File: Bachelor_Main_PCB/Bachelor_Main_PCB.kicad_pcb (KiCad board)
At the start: 2 copper layers, 3 parts, among them J1 F32Q-1A7H1-11022, U1 SC0683

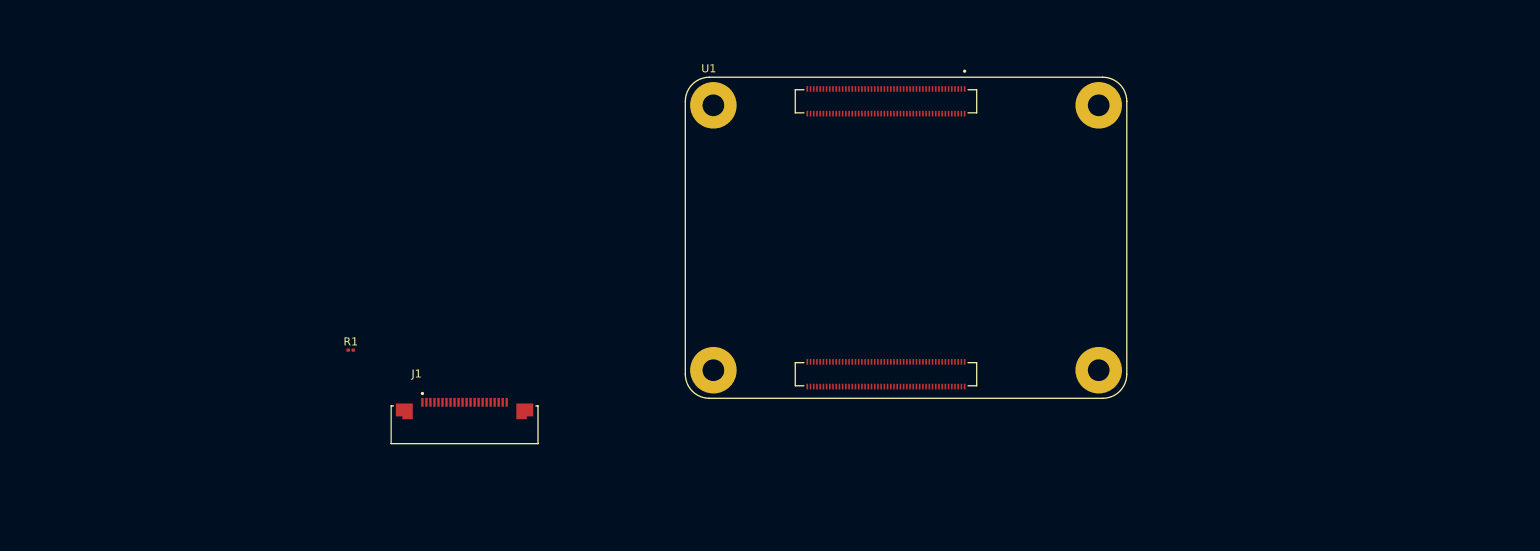
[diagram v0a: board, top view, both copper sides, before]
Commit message: Add Spacers for RPI CM and created separate hierarchical sheets
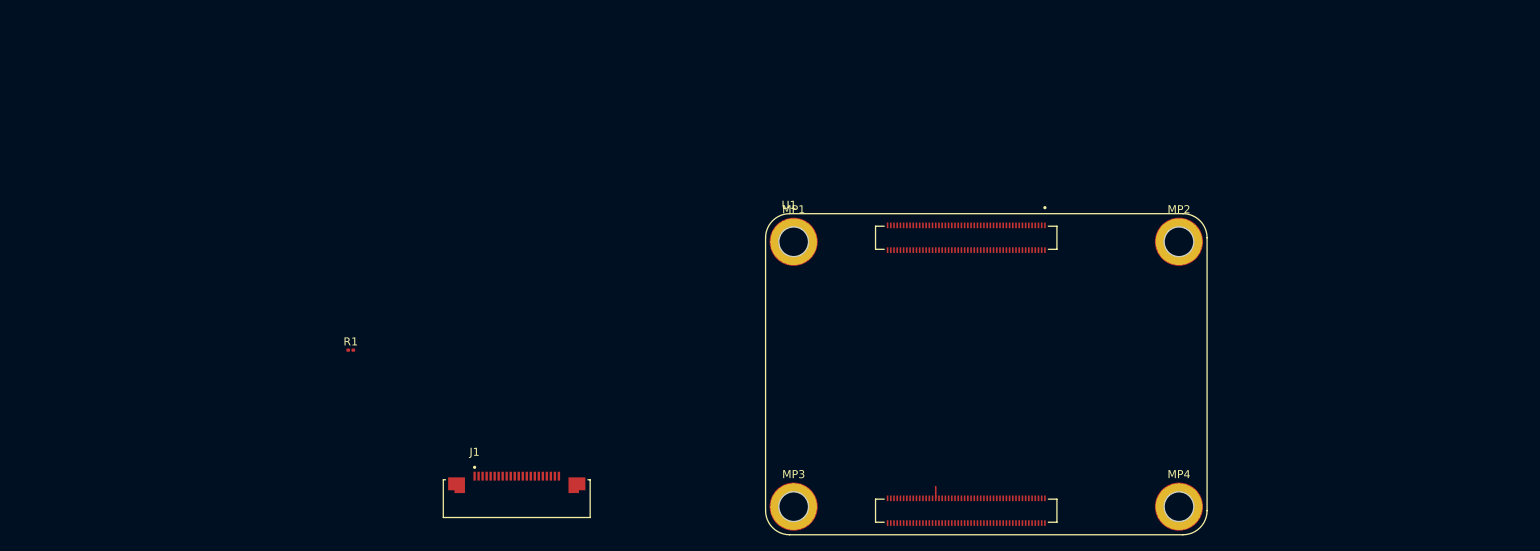
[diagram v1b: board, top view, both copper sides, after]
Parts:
- added MP1: WA-SMSI_9774XXX151, WA-SMSI_9774XXX151:WA-SMSI_9774030151, F.Cu at (159.0, 67.5)
- added MP2: WA-SMSI_9774XXX151, WA-SMSI_9774XXX151:WA-SMSI_9774030151, F.Cu at (207.0, 67.5)
- added MP3: WA-SMSI_9774XXX151, WA-SMSI_9774XXX151:WA-SMSI_9774030151, F.Cu at (159.0, 100.5)
- added MP4: WA-SMSI_9774XXX151, WA-SMSI_9774XXX151:WA-SMSI_9774030151, F.Cu at (207.0, 100.5)
- moved U1 19.7 mm to (183.0, 84.0)
- moved J1 11.3 mm to (124.5, 99.5)
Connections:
- J1 pad 1: unconnected-(J1-Pad1) -> SD-pin6
- J1 pad 10: unconnected-(J1-Pad10) -> SD-pin5
- J1 pad 11: unconnected-(J1-Pad11) -> SD-pin6
- J1 pad 12: unconnected-(J1-Pad12) -> SD-pin4
- J1 pad 13: unconnected-(J1-Pad13) -> SD-pin4
- J1 pad 14: unconnected-(J1-Pad14) -> SD-pin6
- J1 pad 15: unconnected-(J1-Pad15) -> SD-pin3
- J1 pad 16: unconnected-(J1-Pad16) -> SD-pin3
- J1 pad 17: unconnected-(J1-Pad17) -> SD-pin6
- J1 pad 18: unconnected-(J1-Pad18) -> SD-pin2
- J1 pad 19: unconnected-(J1-Pad19) -> SD-pin2
- J1 pad 2: unconnected-(J1-Pad2) -> SD-pin6
- J1 pad 20: unconnected-(J1-Pad20) -> SD-pin6
- J1 pad 21: unconnected-(J1-Pad21) -> SD-pin1
- J1 pad 22: unconnected-(J1-Pad22) -> SD-pin1
- J1 pad 3: unconnected-(J1-Pad3) -> SD-pin8
- J1 pad 4: unconnected-(J1-Pad4) -> SD-pin8
- J1 pad 5: unconnected-(J1-Pad5) -> SD-pin6
- J1 pad 6: unconnected-(J1-Pad6) -> SD-pin7
- J1 pad 7: unconnected-(J1-Pad7) -> SD-pin7
- J1 pad 8: unconnected-(J1-Pad8) -> SD-pin6
- J1 pad 9: unconnected-(J1-Pad9) -> SD-pin5
- R1 pad 2: GND -> SD-pin6
- U1 pad 1: Net-(U1A-GND-Pad1) -> SD-pin6
- U1 pad 107: Net-(U1A-GND-Pad1) -> SD-pin6
- U1 pad 108: Net-(U1A-GND-Pad1) -> SD-pin6
- U1 pad 113: Net-(U1A-GND-Pad1) -> SD-pin6
- U1 pad 114: Net-(U1A-GND-Pad1) -> SD-pin6
- U1 pad 119: Net-(U1A-GND-Pad1) -> SD-pin6
- U1 pad 120: Net-(U1A-GND-Pad1) -> SD-pin6
- U1 pad 125: Net-(U1A-GND-Pad1) -> SD-pin6
- U1 pad 126: Net-(U1A-GND-Pad1) -> SD-pin6
- U1 pad 13: Net-(U1A-GND-Pad1) -> SD-pin6
- U1 pad 131: Net-(U1A-GND-Pad1) -> SD-pin6
- U1 pad 132: Net-(U1A-GND-Pad1) -> SD-pin6
- U1 pad 137: Net-(U1A-GND-Pad1) -> SD-pin6
- U1 pad 138: Net-(U1A-GND-Pad1) -> SD-pin6
- U1 pad 14: Net-(U1A-GND-Pad1) -> SD-pin6
- U1 pad 144: Net-(U1A-GND-Pad1) -> SD-pin6
- U1 pad 150: Net-(U1A-GND-Pad1) -> SD-pin6
- U1 pad 155: Net-(U1A-GND-Pad1) -> SD-pin6
- U1 pad 156: Net-(U1A-GND-Pad1) -> SD-pin6
- U1 pad 161: Net-(U1A-GND-Pad1) -> SD-pin6
- U1 pad 162: Net-(U1A-GND-Pad1) -> SD-pin6
- U1 pad 167: Net-(U1A-GND-Pad1) -> SD-pin6
- U1 pad 168: Net-(U1A-GND-Pad1) -> SD-pin6
- U1 pad 173: Net-(U1A-GND-Pad1) -> SD-pin6
- U1 pad 174: Net-(U1A-GND-Pad1) -> SD-pin6
- U1 pad 179: Net-(U1A-GND-Pad1) -> SD-pin6
- U1 pad 180: Net-(U1A-GND-Pad1) -> SD-pin6
- U1 pad 185: Net-(U1A-GND-Pad1) -> SD-pin6
- U1 pad 186: Net-(U1A-GND-Pad1) -> SD-pin6
- U1 pad 191: Net-(U1A-GND-Pad1) -> SD-pin6
- U1 pad 192: Net-(U1A-GND-Pad1) -> SD-pin6
- U1 pad 197: Net-(U1A-GND-Pad1) -> SD-pin6
- U1 pad 198: Net-(U1A-GND-Pad1) -> SD-pin6
- U1 pad 2: Net-(U1A-GND-Pad1) -> SD-pin6
- U1 pad 22: Net-(U1A-GND-Pad1) -> SD-pin6
- U1 pad 23: Net-(U1A-GND-Pad1) -> SD-pin6
- U1 pad 32: Net-(U1A-GND-Pad1) -> SD-pin6
- U1 pad 33: Net-(U1A-GND-Pad1) -> SD-pin6
- U1 pad 42: Net-(U1A-GND-Pad1) -> SD-pin6
- U1 pad 43: Net-(U1A-GND-Pad1) -> SD-pin6
- U1 pad 52: Net-(U1A-GND-Pad1) -> SD-pin6
- U1 pad 53: Net-(U1A-GND-Pad1) -> SD-pin6
- U1 pad 59: Net-(U1A-GND-Pad1) -> SD-pin6
- U1 pad 60: Net-(U1A-GND-Pad1) -> SD-pin6
- U1 pad 65: Net-(U1A-GND-Pad1) -> SD-pin6
- U1 pad 66: Net-(U1A-GND-Pad1) -> SD-pin6
- U1 pad 7: Net-(U1A-GND-Pad1) -> SD-pin6
- U1 pad 71: Net-(U1A-GND-Pad1) -> SD-pin6
- U1 pad 74: Net-(U1A-GND-Pad1) -> SD-pin6
- U1 pad 8: Net-(U1A-GND-Pad1) -> SD-pin6
- U1 pad 98: Net-(U1A-GND-Pad1) -> SD-pin6
- U1 pad SH1: Net-(U1A-MOUNTING_PADS-PadSH1) -> SD-pin6
- U1 pad SH2: Net-(U1A-MOUNTING_PADS-PadSH1) -> SD-pin6
- U1 pad SH3: Net-(U1A-MOUNTING_PADS-PadSH1) -> SD-pin6
- U1 pad SH4: Net-(U1A-MOUNTING_PADS-PadSH1) -> SD-pin6
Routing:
- net unconnected-(U1B-DSI0_C_N-Pad169): track 0.00 -> 1.46 mm

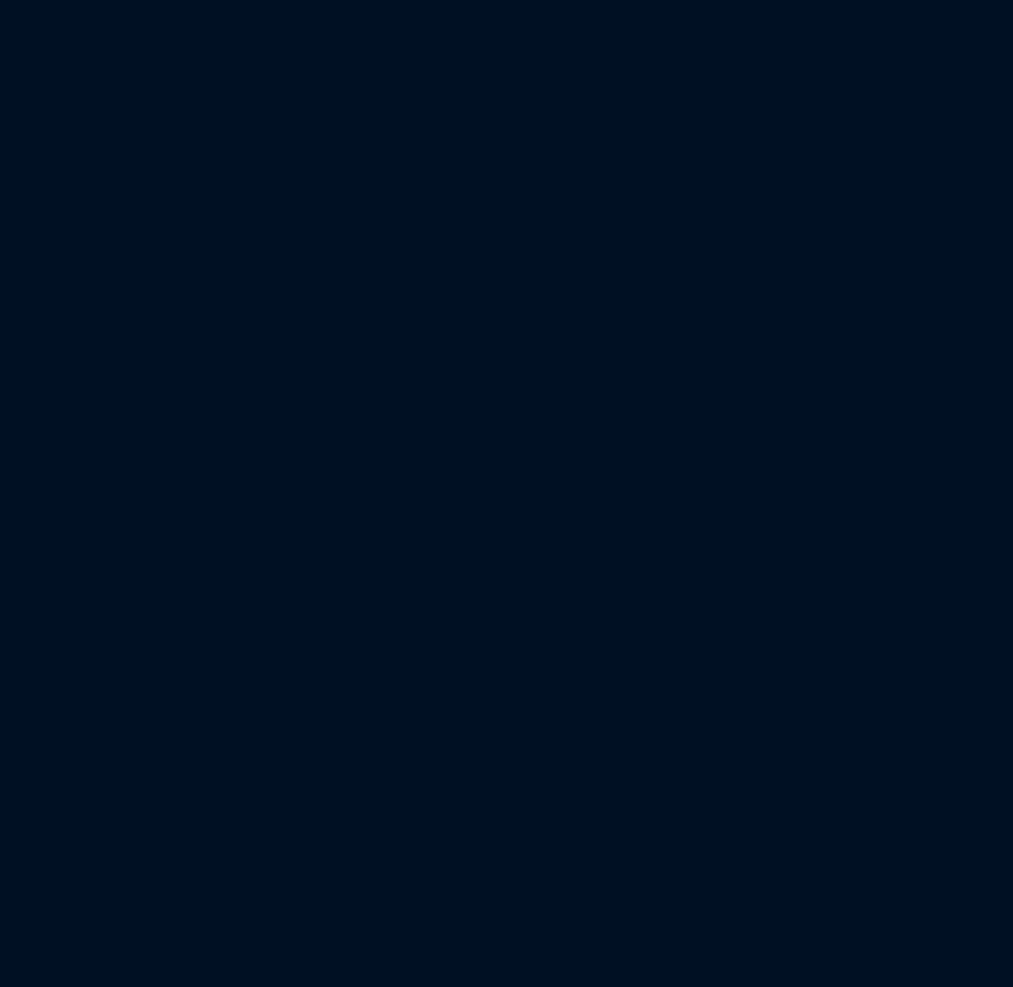
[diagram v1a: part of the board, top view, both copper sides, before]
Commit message: Add Sierra Wireless modem and 100pin RPI CM connectors
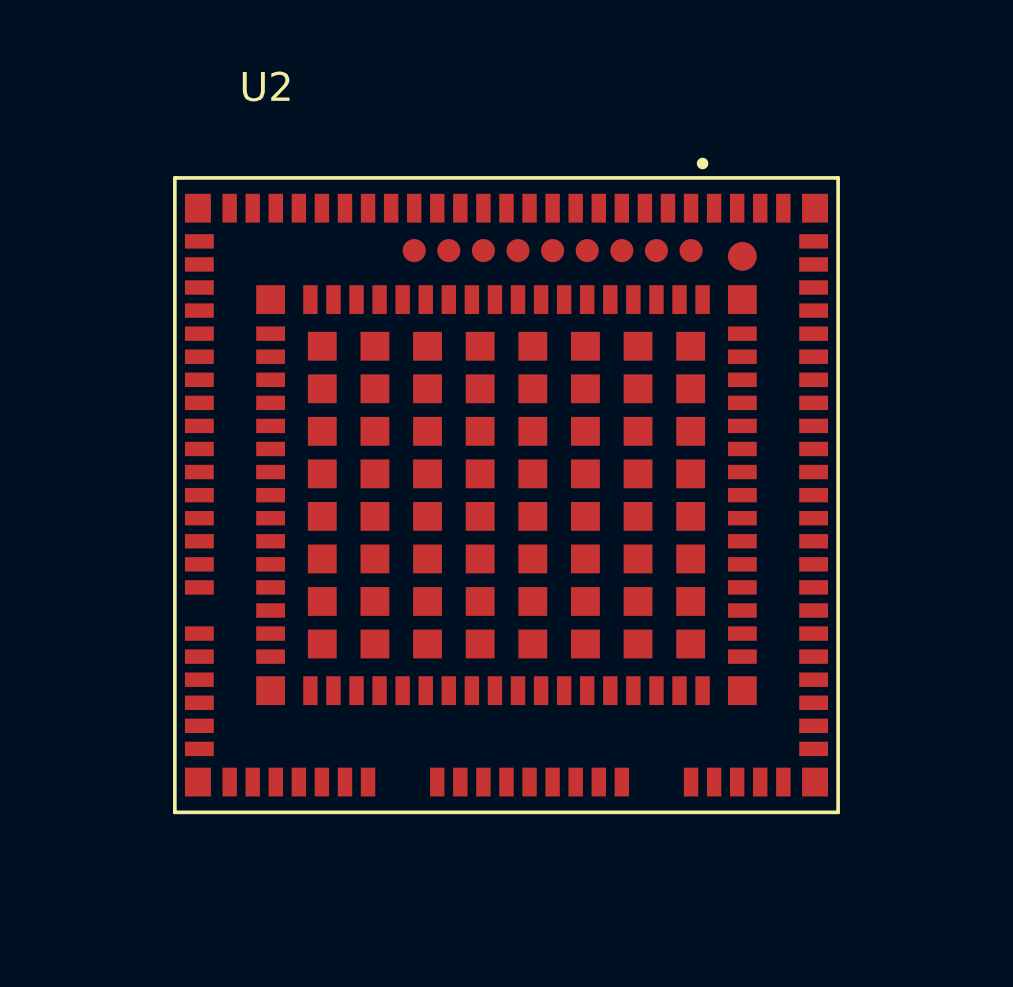
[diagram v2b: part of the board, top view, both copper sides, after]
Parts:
- added U2: RC7620_1104625, RC7620_1104625:XCVR_RC7620_1104625, F.Cu at (124.3, 54.5)

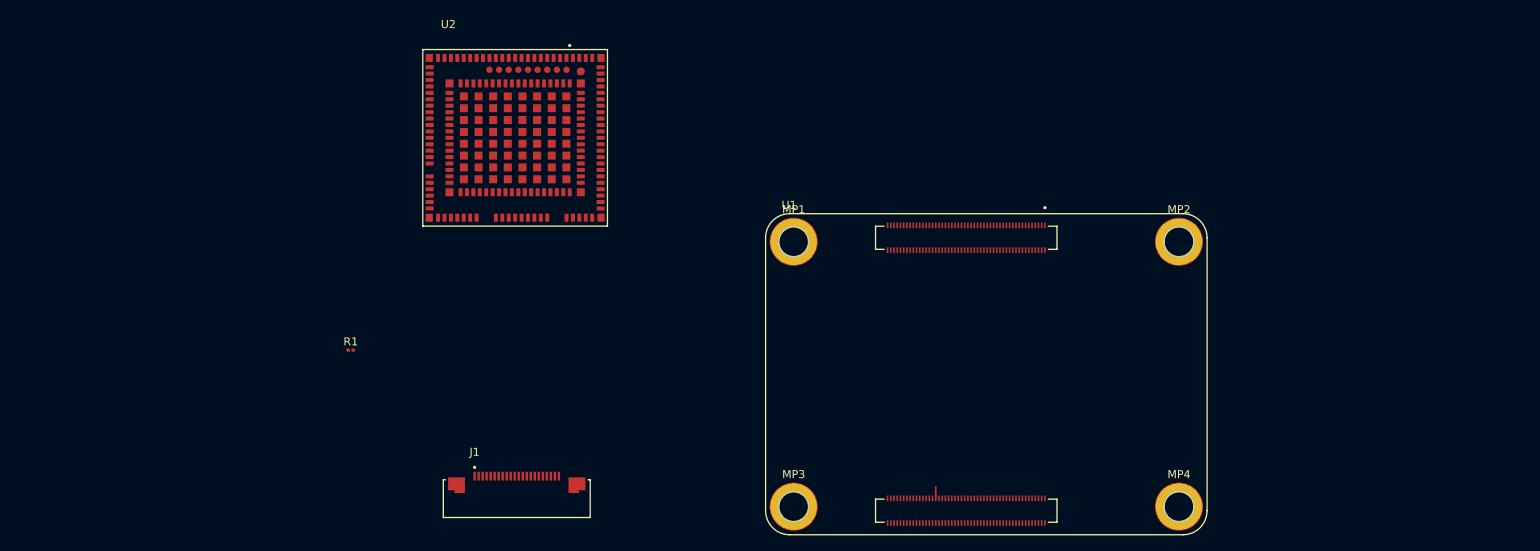
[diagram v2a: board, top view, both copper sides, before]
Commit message: Add STM32 and 3d model. Made power suply sheet
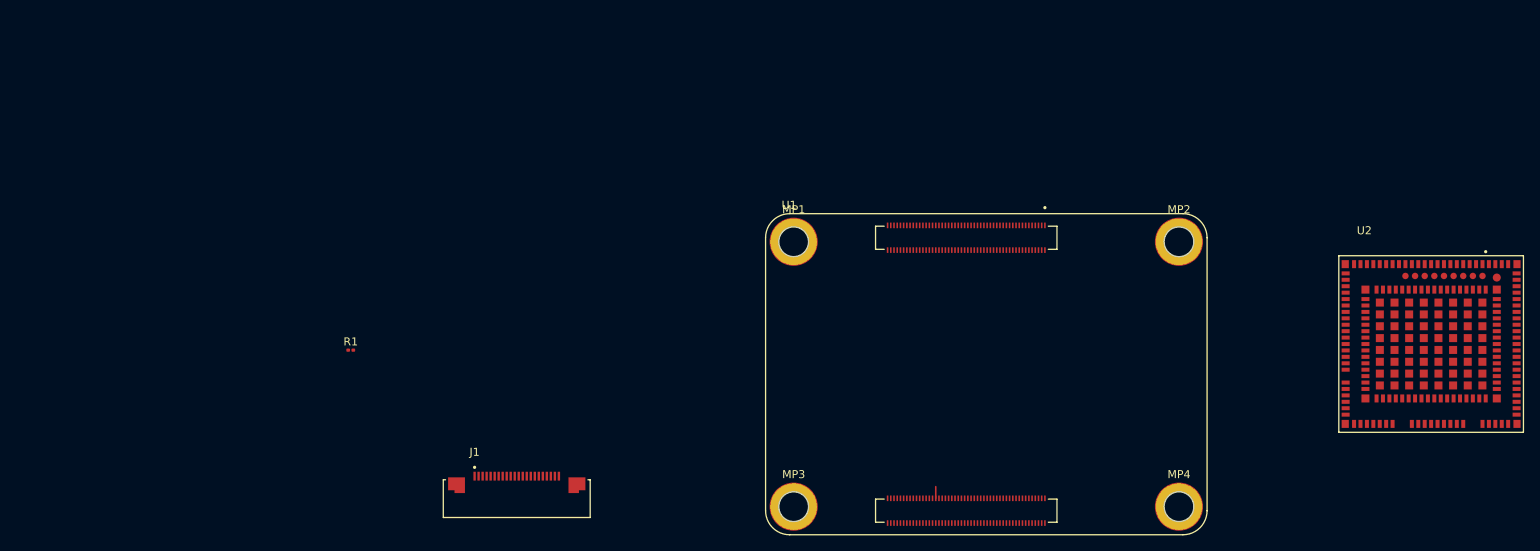
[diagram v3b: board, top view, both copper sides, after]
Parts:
- moved U2 117.0 mm to (238.4, 80.2)
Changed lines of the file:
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@@
+			)
+		)
+		(model "${KICAD9_3DMODEL_DIR}/DF40HC_3.0_-100DS-0.4V_58/DF40HC_3.0_-100DS-0.4V_58.step"
+			(offset
+				(xyz -2.5 -17 0)
+			)
+			(scale
+				(xyz 1 1 1)
+			)
+			(rotate
+				(xyz -90 -0 -0)
+			)
+		)
+		(model "${KICAD9_3DMODEL_DIR}/DF40HC_3.0_-100DS-0.4V_58/DF40HC_3.0_-100DS-0.4V_58.step"
+			(offset
+				(xyz -2.5 17 0)
+			)
+			(scale
+				(xyz 1 1 1)
+			)
+			(rotate
+				(xyz -90 -0 -0)
 			)
 		)
@@
 	(footprint "RC7620_1104625:XCVR_RC7620_1104625"
 		(layer "F.Cu")
-		(at 124.3 54.55)
+		(at 238.4125 80.2375)
 		(property "Reference" "U2"
 			(at -8.325 -14.135 0)

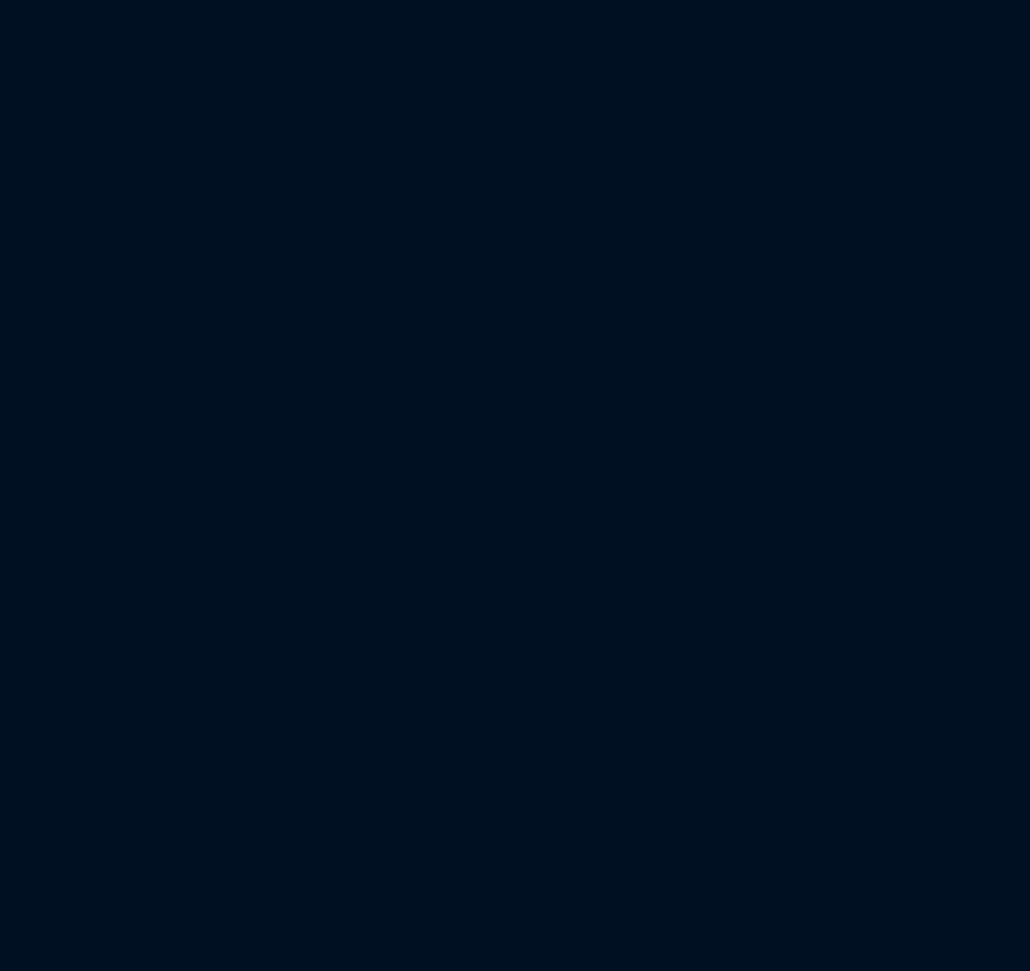
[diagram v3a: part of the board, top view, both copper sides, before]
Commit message: Add STM32 3D modell
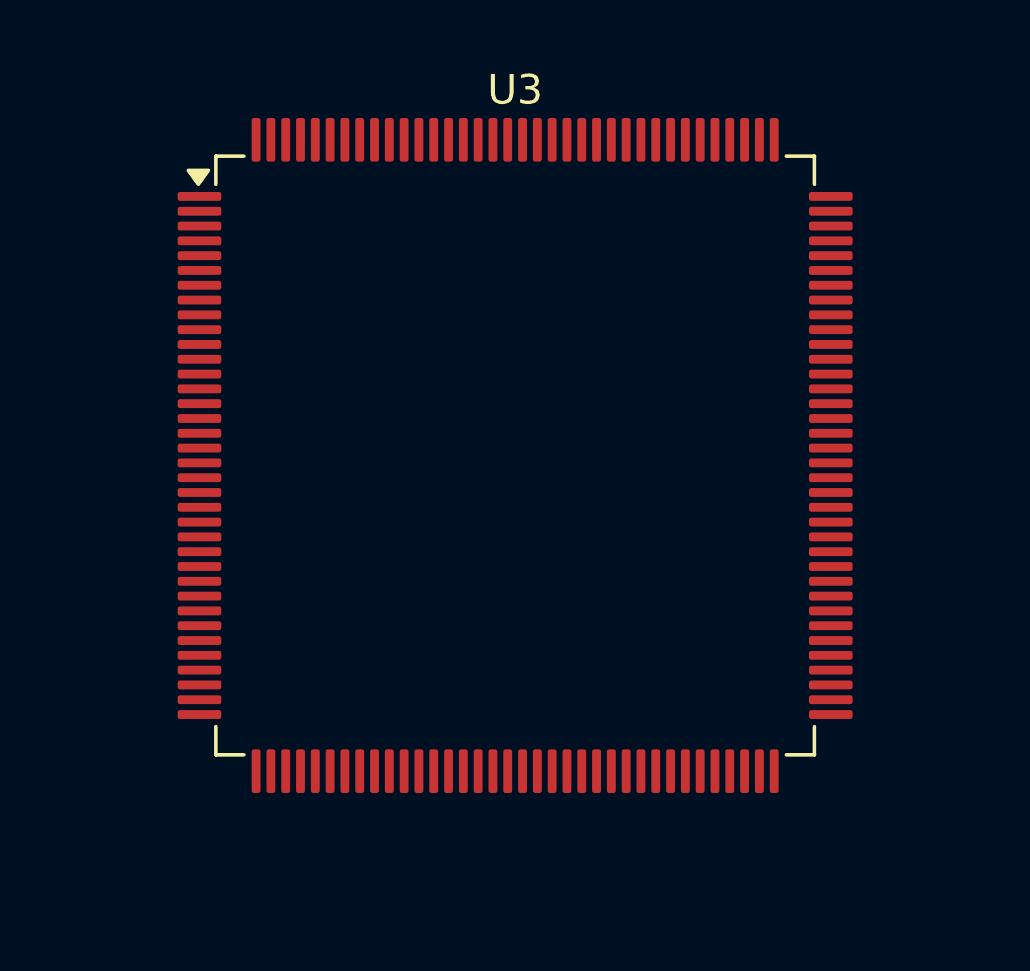
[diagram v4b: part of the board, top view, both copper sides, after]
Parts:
- added U3: STM32H7A3ZITxQ, Package_QFP:LQFP-144_20x20mm_P0.5mm, F.Cu at (125.3, 53.2)
